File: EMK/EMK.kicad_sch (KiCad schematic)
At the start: 53 parts, among them J1 USB_C_Receptacle_USB2.0_14P, J2 Conn_01x02_Socket, J3 Conn_ARM_JTAG_SWD_10, Q1 Si2371EDS, Q2 Si2371EDS, SW1 SW_Nidec_CAS-120A1, SW18 SW_Push, SW19 SW_Nidec_CAS-120A1, U1 nRF52840-QFAA, U2 15nH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

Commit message: Adiciona parte dos Footprints
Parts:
- C1, C13, C14, C15, C16, C17, C18, C19, C2, C20, C21, C3, C4, C6, C8: footprint (none) -> Capacitor_SMD:C_0603_1608Metric
- C10, C11, C12, C5, C9: footprint Capacitor_THT:C_Disc_D5.0mm_W2.5mm_P2.50mm -> Capacitor_SMD:C_0603_1608Metric
- C7: footprint (none) -> Capacitor_SMD:C_0402_1005Metric
- D1: footprint (none) -> Diode_SMD:D_0805_2012Metric
- D2, D3: footprint (none) -> LED_SMD:LED_0603_1608Metric
- L1, L2, U2: footprint (none) -> Inductor_SMD:L_7.3x7.3_H4.5
- L3: footprint (none) -> Inductor_SMD:L_0603_1608Metric
- R1, R2, R3, R4, R5, R6, R7, R8, R9: footprint (none) -> Resistor_SMD:R_0603_1608Metric
- R10: footprint (none) -> Resistor_SMD:R_0603_1608Metrica
- R11: footprint (none) -> Resistor_SMD:R_0402_1005Metric
- SW18: footprint (none) -> Button_Switch_SMD:SW_SPST_B3S-1000
- Y2: footprint (none) -> Crystal:Crystal_SMD_3215-2Pin_3.2x1.5mm
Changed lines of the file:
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@@
 			)
 		)
-		(property "Footprint" ""
+		(property "Footprint" "Capacitor_SMD:C_0603_1608Metric"
 			(at 123.19 143.51 0)
 			(effects
@@
 			)
 		)
-		(property "Footprint" ""
+		(property "Footprint" "Resistor_SMD:R_0603_1608Metric"
 			(at 328.93 145.542 90)
 			(effects
@@
 			)
 		)
-		(property "Footprint" ""
+		(property "Footprint" "Inductor_SMD:L_7.3x7.3_H4.5"
 			(at 166.37 92.71 0)
 			(effects
@@
 			)
 		)
-		(property "Footprint" "Capacitor_THT:C_Disc_D5.0mm_W2.5mm_P2.50mm"
+		(property "Footprint" "Capacitor_SMD:C_0603_1608Metric"
 			(at 146.05 132.08 0)
 			(effects
@@
 		(on_board no)
 		(dnp no)
-		(property "Reference" "GND03"
+		(property "Reference" "#GND03"
 			(at 36.83 93.98 0)
 			(effects
@@
 			(project "EMK"
 				(path "/b49e0e20-ddc2-4eb4-9509-7721d6b2744b"
-					(reference "GND03")
+					(reference "#GND03")
 					(unit 1)
 				)
@@
 			)
 		)
-		(property "Footprint" ""
+		(property "Footprint" "Capacitor_SMD:C_0603_1608Metric"
 			(at 124.46 30.48 0)
 			(effects
@@
 			)
 		)
-		(property "Footprint" ""
+		(property "Footprint" "Resistor_SMD:R_0603_1608Metric"
 			(at 90.932 40.64 90)
 			(effects
@@
 			)
 		)
-		(property "Footprint" ""
+		(property "Footprint" "Resistor_SMD:R_0603_1608Metric"
 			(at 353.06 43.688 90)
 			(effects
@@
 			)
 		)
-		(property "Footprint" ""
+		(property "Footprint" "Resistor_SMD:R_0603_1608Metric"
 			(at 255.27 125.222 90)
 			(effects
@@
 			)
 		)
-		(property "Footprint" ""
+		(property "Footprint" "Crystal:Crystal_SMD_3215-2Pin_3.2x1.5mm"
 			(at 142.24 55.88 0)
 			(effects
@@
 		(on_board no)
 		(dnp no)
-		(property "Reference" "GND05"
+		(property "Reference" "#GND05"
 			(at 123.19 144.78 0)
 			(effects
@@
 			(project "EMK"
 				(path "/b49e0e20-ddc2-4eb4-9509-7721d6b2744b"
-					(reference "GND05")
+					(reference "#GND05")
 					(unit 1)
 				)
@@
 		(dnp no)
 		(fields_autoplaced yes)
-		(property "Reference" "GND08"
+		(property "Reference" "#GND08"
 			(at 149.86 139.7 0)
 			(effects
@@
 			(project "EMK"
 				(path "/b49e0e20-ddc2-4eb4-9509-7721d6b2744b"
-					(reference "GND08")
+					(reference "#GND08")
 					(unit 1)
 				)
@@
 			)
 		)
-		(property "Footprint" ""
+		(property "Footprint" "Resistor_SMD:R_0402_1005Metric"
 			(at 53.848 208.28 90)
 			(effects
@@
 			)
 		)
-		(property "Footprint" ""
+		(property "Footprint" "Capacitor_SMD:C_0603_1608Metric"
 			(at 344.17 108.2548 0)
 			(effects
@@
 			)
 		)
-		(property "Footprint" ""
+		(property "Footprint" "Resistor_SMD:R_0603_1608Metric"
 			(at 100.33 48.768 90)
 			(effects
@@
 			)
 		)
-		(property "Footprint" ""
+		(property "Footprint" "Button_Switch_SMD:SW_SPST_B3S-1000"
 			(at 46.99 127 0)
 			(effects
@@
 			)
 		)
-		(property "Footprint" ""
+		(property "Footprint" "Capacitor_SMD:C_0603_1608Metric"
 			(at 179.07 100.33 0)
 			(effects
@@
 			)
 		)
-		(property "Footprint" ""
+		(property "Footprint" "Diode_SMD:D_0805_2012Metric"
 			(at 259.08 52.07 0)
 			(effects
@@
 		(dnp no)
 		(fields_autoplaced yes)
-		(property "Reference" "GND010"
+		(property "Reference" "#GND010"
 			(at 383.54 57.15 0)
 			(effects
@@
 			(project ""
 				(path "/b49e0e20-ddc2-4eb4-9509-7721d6b2744b"
-					(reference "GND010")
+					(reference "#GND010")
 					(unit 1)
 				)
@@
 			)
 		)
-		(property "Footprint" ""
+		(property "Footprint" "LED_SMD:LED_0603_1608Metric"
 			(at 336.55 143.51 0)
 			(effects
@@
 			)
 		)
-		(property "Footprint" ""
+		(property "Footprint" "Capacitor_SMD:C_0603_1608Metric"
 			(at 151.13 44.45 0)
 			(effects
@@
 			)
 		)
-		(property "Footprint" ""
+		(property "Footprint" "Inductor_SMD:L_0603_1608Metric"
 			(at 267.97 200.66 0)
 			(effects
@@
 			)
 		)
-		(property "Footprint" ""
+		(property "Footprint" "Capacitor_SMD:C_0603_1608Metric"
 			(at 251.46 115.2652 0)
 			(effects
@@
 			)
 		)
-		(property "Footprint" ""
+		(property "Footprint" "Resistor_SMD:R_0603_1608Metric"
 			(at 345.44 46.228 90)
 			(effects
@@
 		(dnp no)
 		(fields_autoplaced yes)
-		(property "Reference" "GND09"
+		(property "Reference" "#GND09"
 			(at 179.07 104.14 0)
 			(effects
@@
 			(project "EMK"
 				(path "/b49e0e20-ddc2-4eb4-9509-7721d6b2744b"
-					(reference "GND09")
+					(reference "#GND09")
 					(unit 1)
 				)
@@
 			)
 		)
-		(property "Footprint" ""
+		(property "Footprint" "Capacitor_SMD:C_0603_1608Metric"
 			(at 251.46 60.6552 0)
 			(effects
@@
 			)
 		)
-		(property "Footprint" ""
+		(property "Footprint" "Resistor_SMD:R_0603_1608Metric"
 			(at 247.65 125.222 90)
 			(effects
@@
 			)
 		)
-		(property "Footprint" ""
+		(property "Footprint" "Resistor_SMD:R_0603_1608Metric"
 			(at 345.44 118.618 90)
 			(effects
@@
 			)
 		)
-		(property "Footprint" ""
+		(property "Footprint" "Capacitor_SMD:C_0603_1608Metric"
 			(at 134.62 30.48 0)
 			(effects
@@
 		(on_board no)
 		(dnp no)
-		(property "Reference" "GND04"
+		(property "Reference" "#GND04"
 			(at 128.27 128.27 0)
 			(effects
@@
 			(project "EMK"
 				(path "/b49e0e20-ddc2-4eb4-9509-7721d6b2744b"
-					(reference "GND04")
+					(reference "#GND04")
 					(unit 1)
 				)
@@
 			)
 		)
-		(property "Footprint" "Capacitor_THT:C_Disc_D5.0mm_W2.5mm_P2.50mm"
+		(property "Footprint" "Capacitor_SMD:C_0603_1608Metric"
 			(at 133.35 132.08 0)
 			(effects
@@
 			)
 		)
-		(property "Footprint" "Capacitor_THT:C_Disc_D5.0mm_W2.5mm_P2.50mm"
+		(property "Footprint" "Capacitor_SMD:C_0603_1608Metric"
 			(at 158.75 78.74 0)
 			(effects
@@
 			)
 		)
-		(property "Footprint" "Capacitor_THT:C_Disc_D5.0mm_W2.5mm_P2.50mm"
+		(property "Footprint" "Capacitor_SMD:C_0603_1608Metric"
 			(at 158.75 132.08 0)
 			(effects
@@
 			)
 		)
-		(property "Footprint" ""
+		(property "Footprint" "Inductor_SMD:L_7.3x7.3_H4.5"
 			(at 176.53 92.71 0)
 			(effects
@@
 			)
 		)
-		(property "Footprint" ""
+		(property "Footprint" "Capacitor_SMD:C_0603_1608Metric"
 			(at 247.65 139.3952 0)
 			(effects
@@
 			)
 		)
-		(property "Footprint" ""
+		(property "Footprint" "Capacitor_SMD:C_0402_1005Metric"
 			(at 118.11 127 0)
 			(effects
@@
 			)
 		)
-		(property "Footprint" ""
+		(property "Footprint" "LED_SMD:LED_0603_1608Metric"
 			(at 341.63 143.51 0)
 			(effects
@@
 		(on_board no)
 		(dnp no)
-		(property "Reference" "GND02"
+		(property "Reference" "#GND02"
 			(at 156.21 34.29 0)
 			(effects
@@
 			(project "EMK"
 				(path "/b49e0e20-ddc2-4eb4-9509-7721d6b2744b"
-					(reference "GND02")
+					(reference "#GND02")
 					(unit 1)
 				)
@@
 			)
 		)
-		(property "Footprint" "Capacitor_THT:C_Disc_D5.0mm_W2.5mm_P2.50mm"
+		(property "Footprint" "Capacitor_SMD:C_0603_1608Metric"
 			(at 132.08 127 0)
 			(effects
@@
 		(on_board no)
 		(dnp no)
-		(property "Reference" "GND06"
+		(property "Reference" "#GND06"
 			(at 118.11 128.27 0)
 			(effects
@@
 			(project "EMK"
 				(path "/b49e0e20-ddc2-4eb4-9509-7721d6b2744b"
-					(reference "GND06")
+					(reference "#GND06")
 					(unit 1)
 				)
@@
 			)
 		)
-		(property "Footprint" ""
+		(property "Footprint" "Capacitor_SMD:C_0603_1608Metric"
 			(at 143.51 44.45 0)
 			(effects
@@
 		(dnp no)
 		(fields_autoplaced yes)
-		(property "Reference" "GND07"
+		(property "Reference" "#GND07"
 			(at 182.88 66.04 0)
 			(effects
@@
 			(project "EMK"
 				(path "/b49e0e20-ddc2-4eb4-9509-7721d6b2744b"
-					(reference "GND07")
+					(reference "#GND07")
 					(unit 1)
 				)
@@
 			)
 		)
-		(property "Footprint" ""
+		(property "Footprint" "Capacitor_SMD:C_0603_1608Metric"
 			(at 260.0452 208.28 0)
 			(effects
@@
 			)
 		)
-		(property "Footprint" ""
+		(property "Footprint" "Capacitor_SMD:C_0603_1608Metric"
 			(at 240.9952 208.28 0)
 			(effects
@@
 			)
 		)
-		(property "Footprint" ""
+		(property "Footprint" "Capacitor_SMD:C_0603_1608Metric"
 			(at 173.99 78.74 0)
 			(effects
@@
 		(on_board no)
 		(dnp no)
-		(property "Reference" "GND01"
+		(property "Reference" "#GND01"
 			(at 140.97 20.32 0)
 			(effects
@@
 			(project "EMK"
 				(path "/b49e0e20-ddc2-4eb4-9509-7721d6b2744b"
-					(reference "GND01")
+					(reference "#GND01")
 					(unit 1)
 				)
@@
 			)
 		)
-		(property "Footprint" ""
+		(property "Footprint" "Inductor_SMD:L_7.3x7.3_H4.5"
 			(at 259.08 109.22 0)
 			(effects
@@
 			)
 		)
-		(property "Footprint" ""
+		(property "Footprint" "Resistor_SMD:R_0603_1608Metrica"
 			(at 248.92 202.438 90)
 			(effects
@@
 			)
 		)
-		(property "Footprint" ""
+		(property "Footprint" "Capacitor_SMD:C_0603_1608Metric"
 			(at 251.46 73.3552 0)
 			(effects
@@
 			)
 		)
-		(property "Footprint" ""
+		(property "Footprint" "Capacitor_SMD:C_0603_1608Metric"
 			(at 280.3652 208.28 0)
 			(effects
@@
 			)
 		)
-		(property "Footprint" ""
+		(property "Footprint" "Resistor_SMD:R_0603_1608Metric"
 			(at 255.27 42.672 90)
 			(effects

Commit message: Roteamento da MCU e posicionamento
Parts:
- added AE1: Antenna, RF_Antenna:Johanson_2450AT43F0100, symbol Device:Antenna
- R10: footprint Resistor_SMD:R_0603_1608Metrica -> Resistor_SMD:R_0603_1608Metric
- Y1: footprint Crystal:Crystal_AT310_D3.0mm_L10.0mm_Horizontal -> Crystal:Crystal_SMD_2012-2Pin_2.0x1.2mm
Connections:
- net ANT_TRACE: no longer names the net of C19.1, R10.1
- net ANT_TRACE: now also AE1.1 (A)
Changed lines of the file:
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@@
 	(wire
 		(pts
+			(xy 226.06 200.66) (xy 240.03 200.66)
+		)
+		(stroke
+			(width 0)
+			(type default)
+		)
+	)
+	(wire
+		(pts
 			(xy 31.75 86.36) (xy 36.83 86.36)
 		)
@@
 	(wire
 		(pts
-			(xy 232.41 200.66) (xy 240.03 200.66)
+			(xy 179.07 92.71) (xy 179.07 97.79)
 		)
 		(stroke
@@
 	(wire
 		(pts
-			(xy 179.07 92.71) (xy 179.07 97.79)
+			(xy 41.91 121.92) (xy 38.1 121.92)
 		)
 		(stroke
@@
 	(wire
 		(pts
-			(xy 41.91 121.92) (xy 38.1 121.92)
+			(xy 160.02 92.71) (xy 156.21 92.71)
 		)
 		(stroke
@@
 	(wire
 		(pts
-			(xy 160.02 92.71) (xy 156.21 92.71)
+			(xy 36.83 93.98) (xy 36.83 90.17)
 		)
 		(stroke
@@
 	(wire
 		(pts
-			(xy 36.83 93.98) (xy 36.83 90.17)
+			(xy 226.06 200.66) (xy 226.06 190.5)
 		)
 		(stroke
@@
 		)
 	)
-	(global_label "ANT_TRACE"
-		(shape input)
-		(at 232.41 200.66 180)
-		(fields_autoplaced yes)
-		(effects
-			(font
-				(size 1.27 1.27)
-			)
-			(justify right)
-		)
-		(property "Intersheetrefs" "${INTERSHEET_REFS}"
-			(at 219.3253 200.66 0)
-			(effects
-				(font
-					(size 1.27 1.27)
-				)
-				(justify right)
-				(hide yes)
-			)
-		)
-	)
 	(global_label "VBUS"
 		(shape input)
@@
 			)
 		)
-		(property "Footprint" "Crystal:Crystal_AT310_D3.0mm_L10.0mm_Horizontal"
+		(property "Footprint" "Crystal:Crystal_SMD_2012-2Pin_2.0x1.2mm"
 			(at 124.46 43.18 0)
 			(effects
@@
 	)
 	(symbol
+		(lib_id "Device:Antenna")
+		(at 226.06 185.42 0)
+		(unit 1)
+		(exclude_from_sim no)
+		(in_bom yes)
+		(on_board yes)
+		(dnp no)
+		(fields_autoplaced yes)
+		(property "Reference" "AE1"
+			(at 228.6 184.7849 0)
+			(effects
+				(font
+					(size 1.27 1.27)
+				)
+				(justify left)
+			)
+		)
+		(property "Value" "Antenna"
+			(at 228.6 187.3249 0)
+			(effects
+				(font
+					(size 1.27 1.27)
+				)
+				(justify left)
+			)
+		)
+		(property "Footprint" "RF_Antenna:Johanson_2450AT43F0100"
+			(at 226.06 185.42 0)
+			(effects
+				(font
+					(size 1.27 1.27)
+				)
+				(hide yes)
+			)
+		)
+		(property "Datasheet" "~"
+			(at 226.06 185.42 0)
+			(effects
+				(font
+					(size 1.27 1.27)
+				)
+				(hide yes)
+			)
+		)
+		(property "Description" "Antenna"
+			(at 226.06 185.42 0)
+			(effects
+				(font
+					(size 1.27 1.27)
+				)
+				(hide yes)
+			)
+		)
+		(pin "1"
+		)
+		(instances
+			(project ""
+				(path "/b49e0e20-ddc2-4eb4-9509-7721d6b2744b"
+					(reference "AE1")
+					(unit 1)
+				)
+			)
+		)
+	)
+	(symbol
 		(lib_id "Device:R")
 		(at 52.07 208.28 180)
@@
 			)
 		)
-		(property "Footprint" "Resistor_SMD:R_0603_1608Metrica"
+		(property "Footprint" "Resistor_SMD:R_0603_1608Metric"
 			(at 248.92 202.438 90)
 			(effects

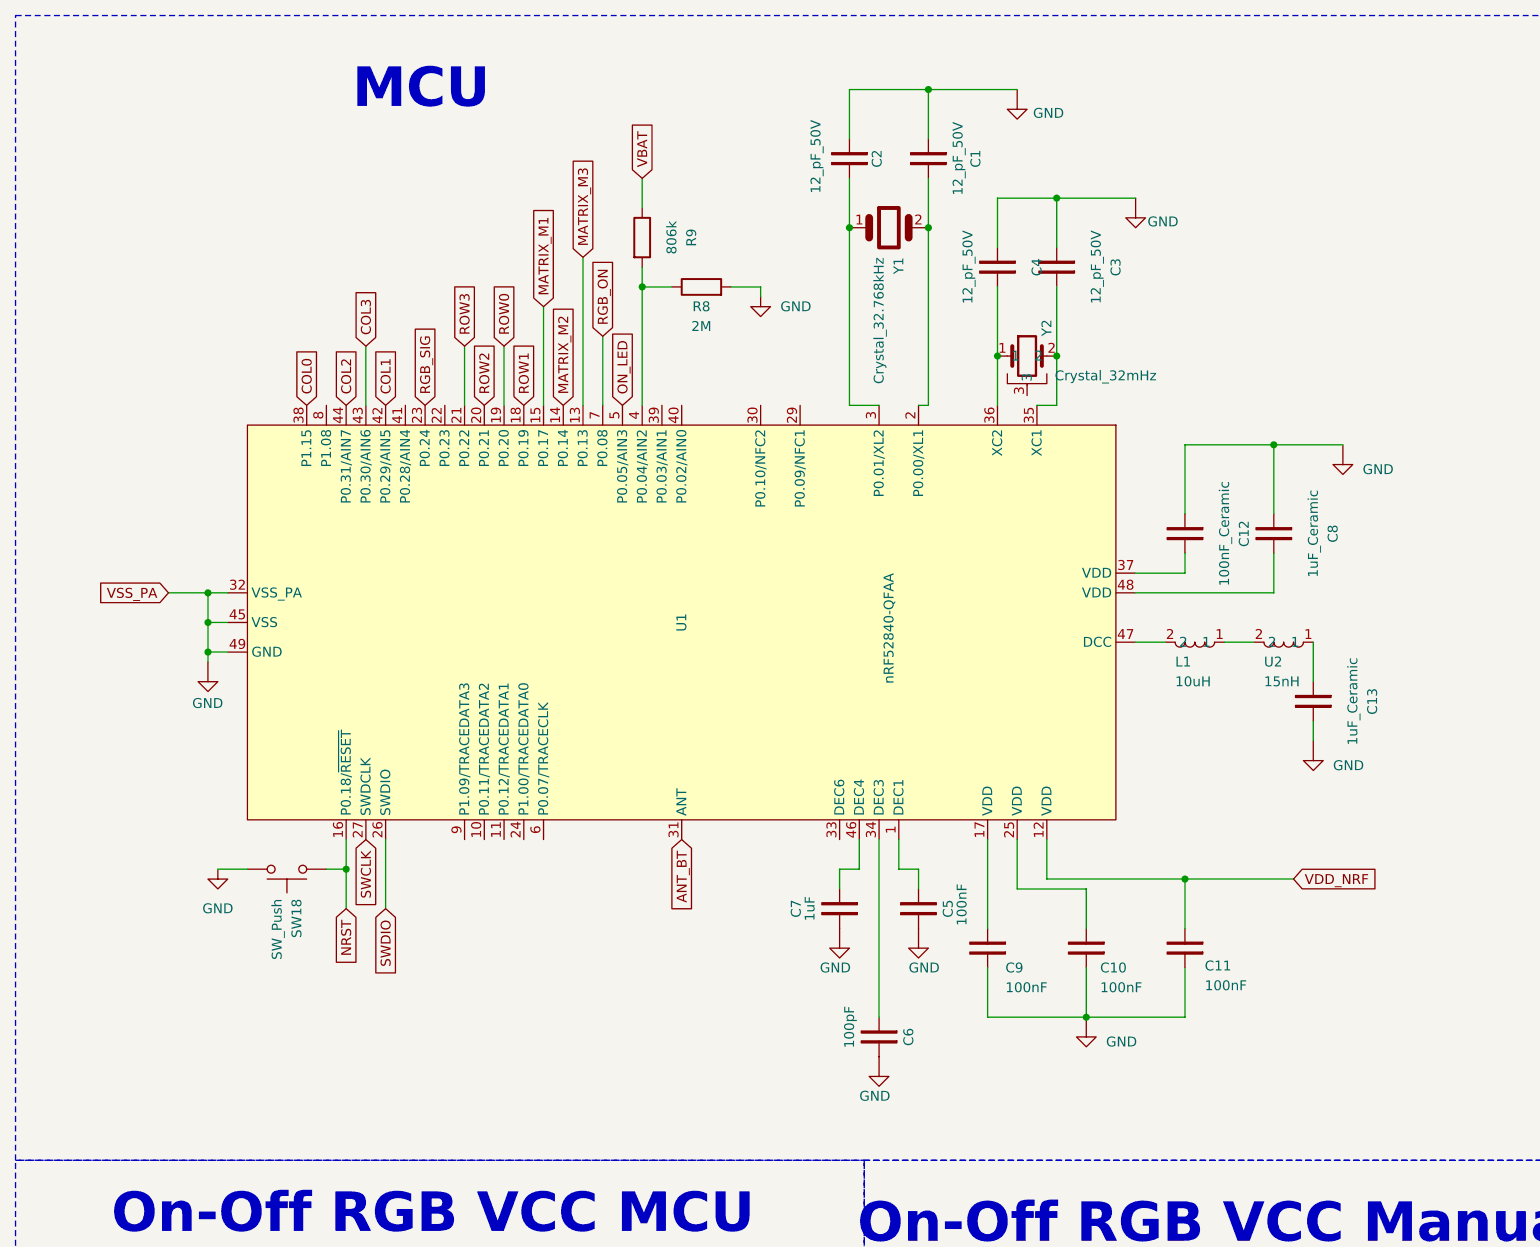
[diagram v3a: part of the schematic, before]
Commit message: feat: realiza o roteamento das trilhas da matriz e dos leds.
Signed-off-by: Paulo Santos <prms@ic.ufal.br>
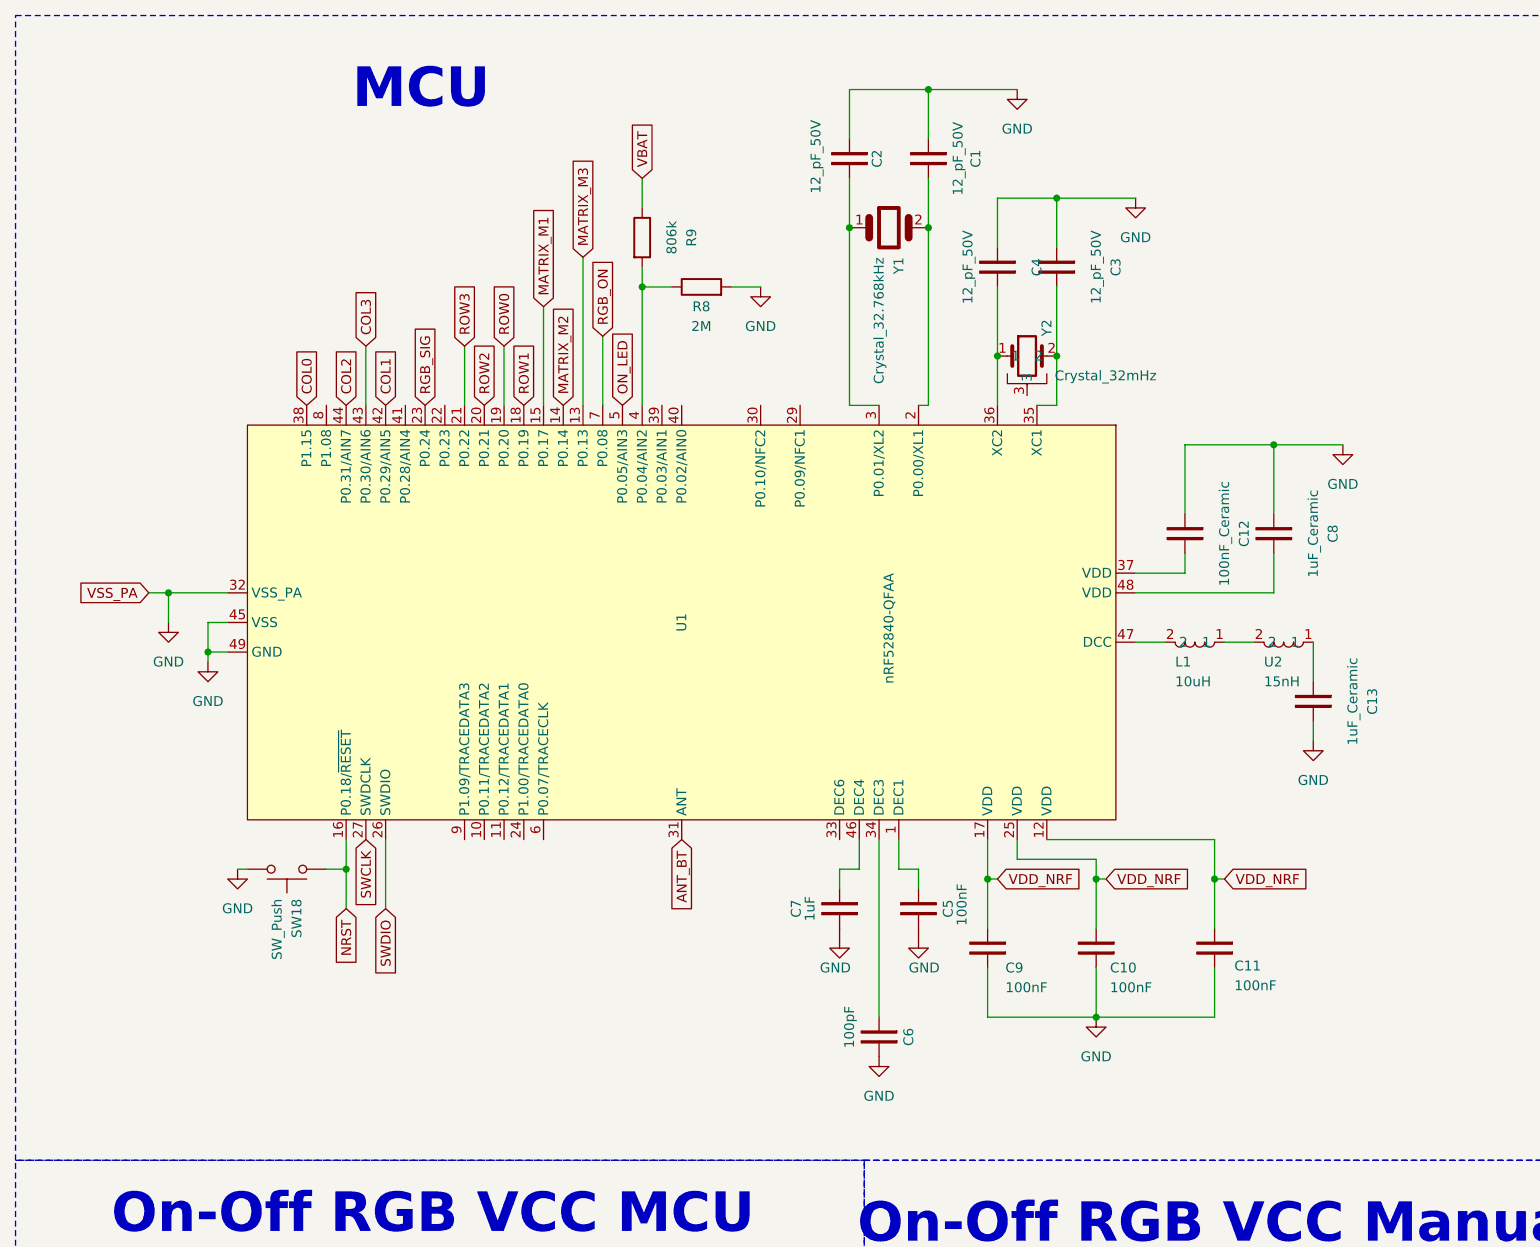
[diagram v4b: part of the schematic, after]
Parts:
- J1: footprint (none) -> Connector_USB:USB_C_Receptacle_XKB_U262-16XN-4BVC11
- J2: footprint (none) -> Connector_PinHeader_2.54mm:PinHeader_1x02_P2.54mm_Horizontal
- L1, U2: footprint Inductor_SMD:L_7.3x7.3_H4.5 -> Inductor_SMD:L_0603_1608Metric
- SW18: footprint Button_Switch_SMD:SW_SPST_B3S-1000 -> Button_Switch_SMD:SW_SPST_B3U-1000P
- U5: footprint Package_TO_SOT_SMD:TSOT-23-5 -> Package_TO_SOT_SMD:TSOT-23-6
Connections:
- net VSS_PA is gone; now on net GND: C21.2, U1.32 (VSS_PA), U1.45 (VSS), U1.49 (GND)
- net GND: now also C1.1, C10.2, C11.2, C12.1, C13.2, C2.1, C3.1, C4.1, C6.2, C8.1, C9.2
- net VDD_NRF: now also C10.1, C9.1, U1.17 (VDD), U1.25 (VDD)
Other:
- moved on the sheet: C10, C11

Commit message: Roteamento
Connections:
- net GND: now also C5.1, C7.2

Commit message: Remap tracement
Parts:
- removed C19: 1.5pF, Capacitor_SMD:C_0603_1608Metric, symbol Device:C
- removed R10: 0, Resistor_SMD:R_0603_1608Metric, symbol Device:R
- removed U4: USBLC6-2SC6, Package_TO_SOT_SMD:SOT-23-6, symbol EMKPower:USBLC6-2SC6
- added L4: 2.7nH, Inductor_SMD:L_0603_1608Metric, symbol Device:L
- AE1: footprint RF_Antenna:Johanson_2450AT43F0100 -> RF_Antenna:Johanson_2450AT18x100
- J3: footprint (none) -> LED:ARM_SWD_SMD_TH
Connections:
- net ANT_BT: now also C20.2; no longer L3.2
- net COL1: now also U1.39 (P0.03/AIN1); no longer U1.42 (P0.29/AIN5)
- net COL2: now also U1.40 (P0.02/AIN0); no longer U1.44 (P0.31/AIN7)
- net COL3: now also U1.41 (P0.28/AIN4); no longer U1.43 (P0.30/AIN6)
- net GND: now also L4.1; no longer C20.2
- net RGB_SIG: now also U1.8 (P1.08); no longer U1.23 (P0.24)
- net ROW0: now also U1.42 (P0.29/AIN5); no longer U1.19 (P0.20)
- net ROW1: now also U1.43 (P0.30/AIN6); no longer U1.18 (P0.19)
- net ROW2: now also U1.44 (P0.31/AIN7)
- net ROW3: now also U1.6 (P0.07/TRACECLK); no longer U1.21 (P0.22)
- net at AE1.1 (A): now also L3.1
- net at C20.1: now also L3.2, L4.2; no longer L3.1
- net J_D+: no longer names the net of J1.A6 (D+)
- net J_D+: no longer J1.B6 (D+)
- net J_D-: no longer names the net of J1.A7 (D-)
- net J_D-: no longer J1.B7 (D-)
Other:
- moved on the sheet: C20, L3
